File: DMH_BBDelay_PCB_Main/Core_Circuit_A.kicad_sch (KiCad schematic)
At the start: 99 parts, among them J22 Conn_01x04, J23 Conn_01x04, J24 Conn_01x04, J25 Conn_01x04, J26 Conn_01x08, J27 Conn_01x08, J28 Conn_01x08, J29 Conn_01x08, J34 Conn_01x04, J35 Conn_01x02, J38 Conn_01x08, J39 Conn_01x04, Q19 BC548, Q3 J113, SW3 SW_SPDT, U1 TL074, U2 TL074, U22 V3205, U24 V3205, U25 V3205, U28 40106, U29 TL072, U3 V3205, U4 CD4046, U9 40106

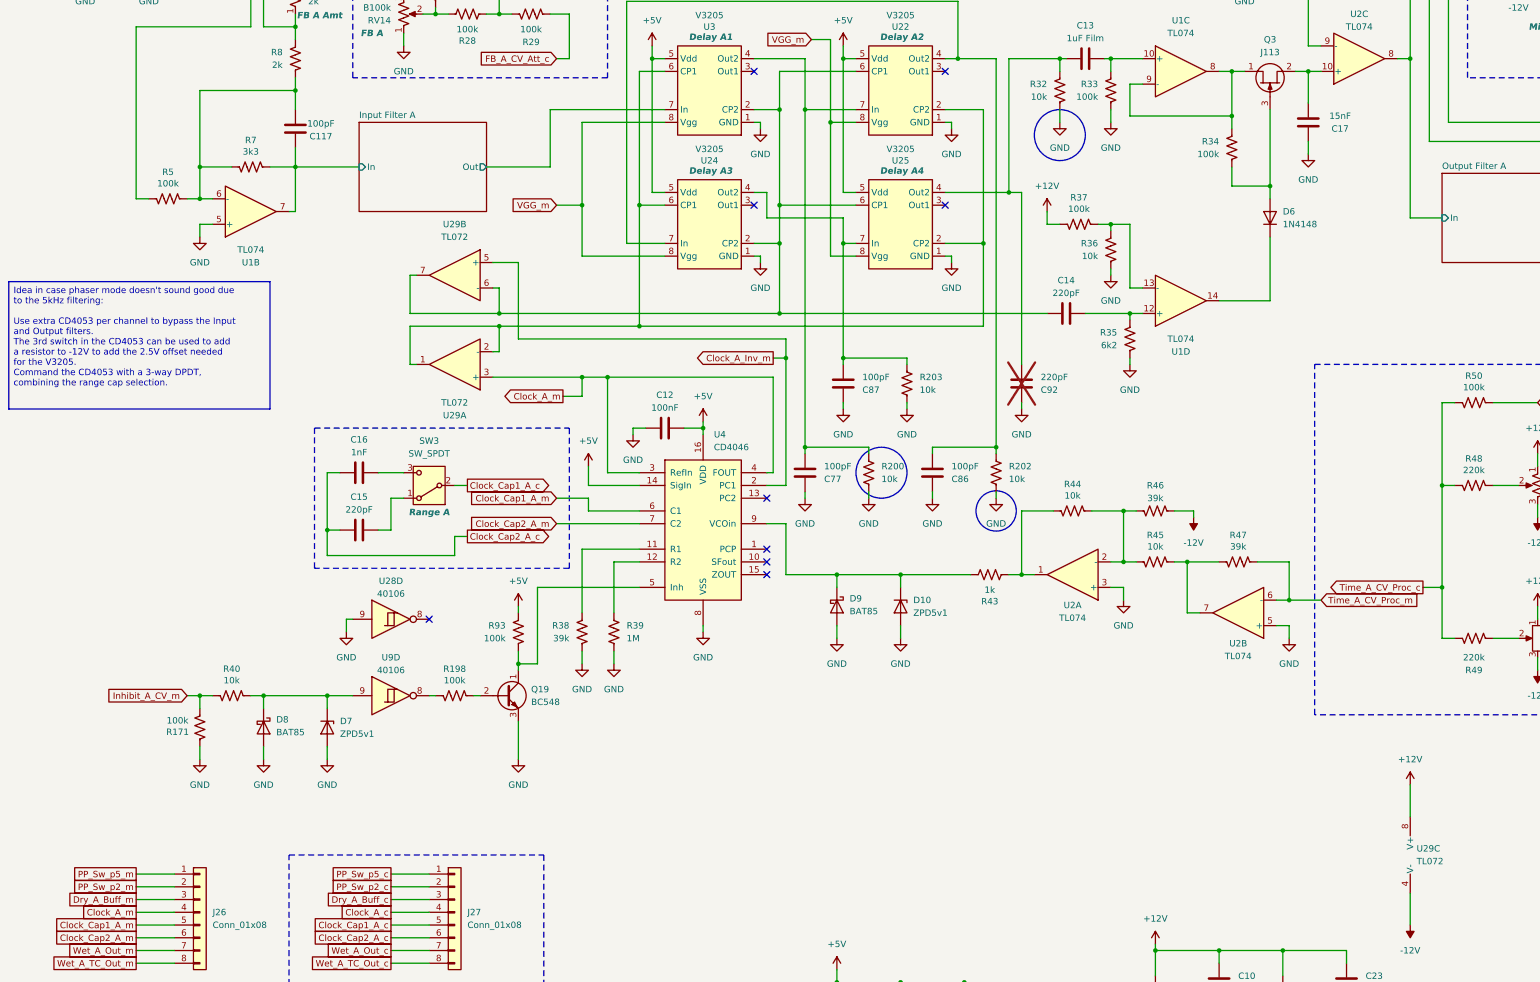
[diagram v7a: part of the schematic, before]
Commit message: Replaced CD40106 with TL074 as clock buffer
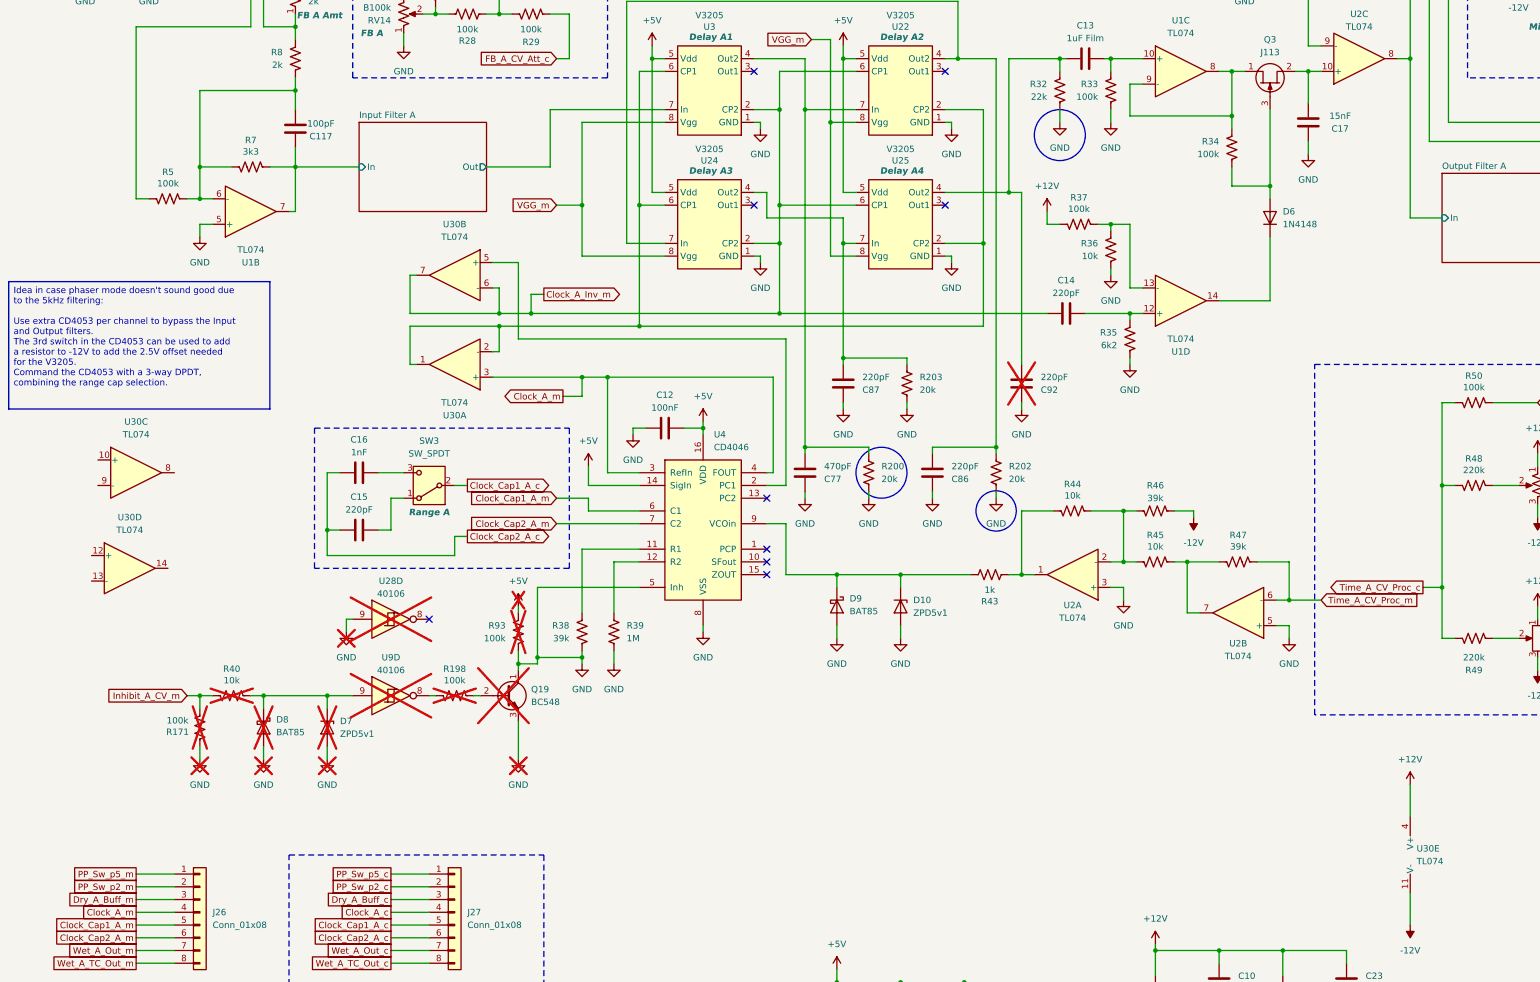
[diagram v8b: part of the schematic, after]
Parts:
- removed U29: TL072, Package_DIP:DIP-8_W7.62mm_Socket, symbol Amplifier_Operational:TL072
- added U30: TL074, Package_DIP:DIP-14_W7.62mm_Socket, symbol Amplifier_Operational:TL074
- C77: value 100pF -> 470pF
- C86, C87: value 100pF -> 220pF
- D7, D8, Q19, R171, R198, R40, R93, U28, U9: now not fitted
- R200, R202, R203: value 10k -> 20k
- R32: value 10k -> 22k
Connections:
- net +12V: now also U30.4 (V+)
- net -12V: now also U30.11 (V-)
- net Clock_A_Inv_m: now also C14.1, U22.6 (CP1), U24.2 (CP2), U25.6 (CP1), U3.2 (CP2), U30.6 (-), U30.7; no longer U4.2 (PC1)
- net Clock_A_m: now also U30.3 (+)
- net GND: now also Q19.1 (C), R93.1, U4.5 (Inh)
- net at U22.2 (CP2), U24.6 (CP1), U25.2 (CP2)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: now also U30.1, U30.2 (-)
- new net: U30.5 (+), U4.2 (PC1)
